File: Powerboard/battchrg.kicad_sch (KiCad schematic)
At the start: 62 parts, among them J1 Thermistor Connection 103AT N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, Q1 SI7617DN-T1-GE3, Q2 SI7617DN-T1-GE3, Q3 SI7617DN-T1-GE3, Q4 SIS412DN-T1-GE3-iclr, Q5 SIS412DN-T1-GE3-iclr

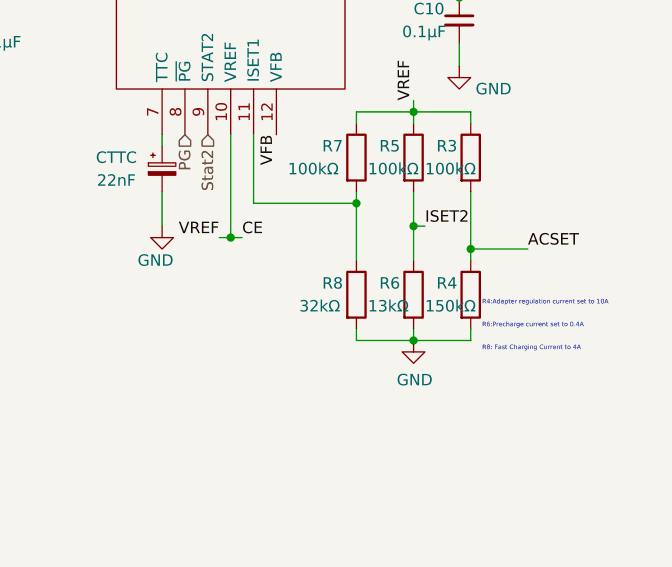
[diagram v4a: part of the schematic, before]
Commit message: removed battery monitor
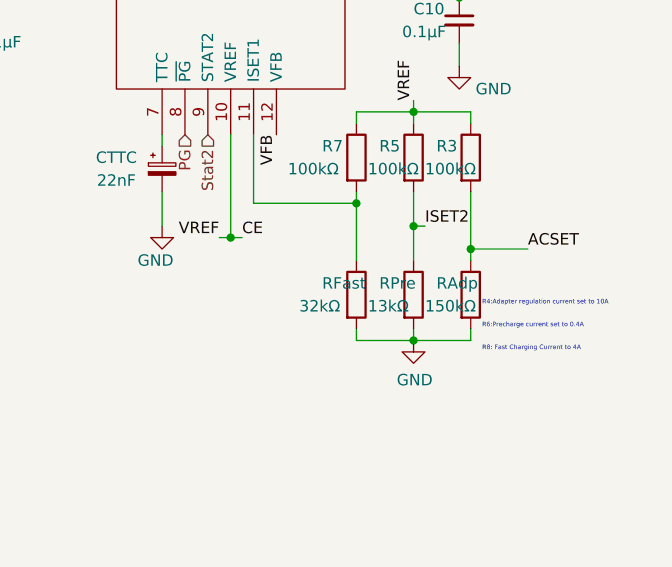
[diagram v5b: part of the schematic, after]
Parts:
- renumbered R4 to RAdp, R8 to RFast, R6 to RPre
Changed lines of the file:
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@@
   (symbol (lib_id "Device:R") (at 241.3 151.13 0) (unit 1)
     (in_bom yes) (on_board yes)
-    (property "Reference" "R8" (id 0) (at 237.49 149.86 0)
+    (property "Reference" "RFast" (id 0) (at 237.49 149.86 0)
       (effects (font (size 1.27 1.27)) (justify left))
     )
@@
   (symbol (lib_id "Device:R") (at 254 151.13 0) (unit 1)
     (in_bom yes) (on_board yes)
-    (property "Reference" "R4" (id 0) (at 250.19 149.86 0)
+    (property "Reference" "RAdp" (id 0) (at 250.19 149.86 0)
       (effects (font (size 1.27 1.27)) (justify left))
     )
@@
   (symbol (lib_id "Device:R") (at 247.65 151.13 0) (unit 1)
     (in_bom yes) (on_board yes)
-    (property "Reference" "R6" (id 0) (at 243.84 149.86 0)
+    (property "Reference" "RPre" (id 0) (at 243.84 149.86 0)
       (effects (font (size 1.27 1.27)) (justify left))
     )

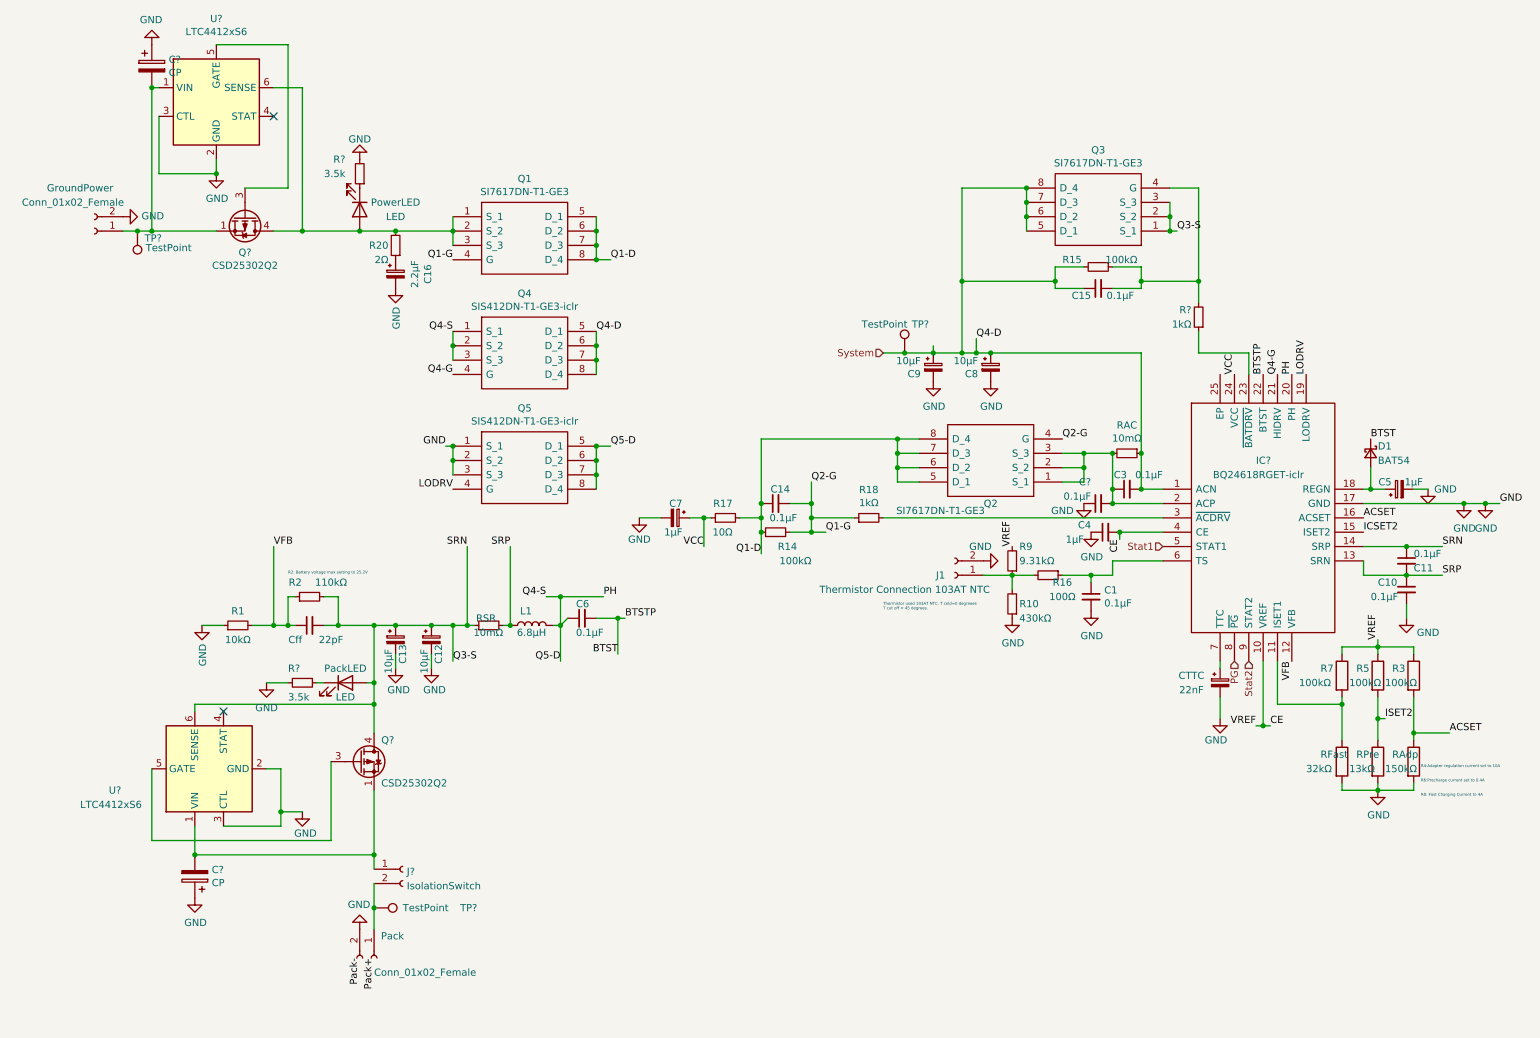
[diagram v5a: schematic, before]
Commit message: Added connectors and potential divider for charge measurement
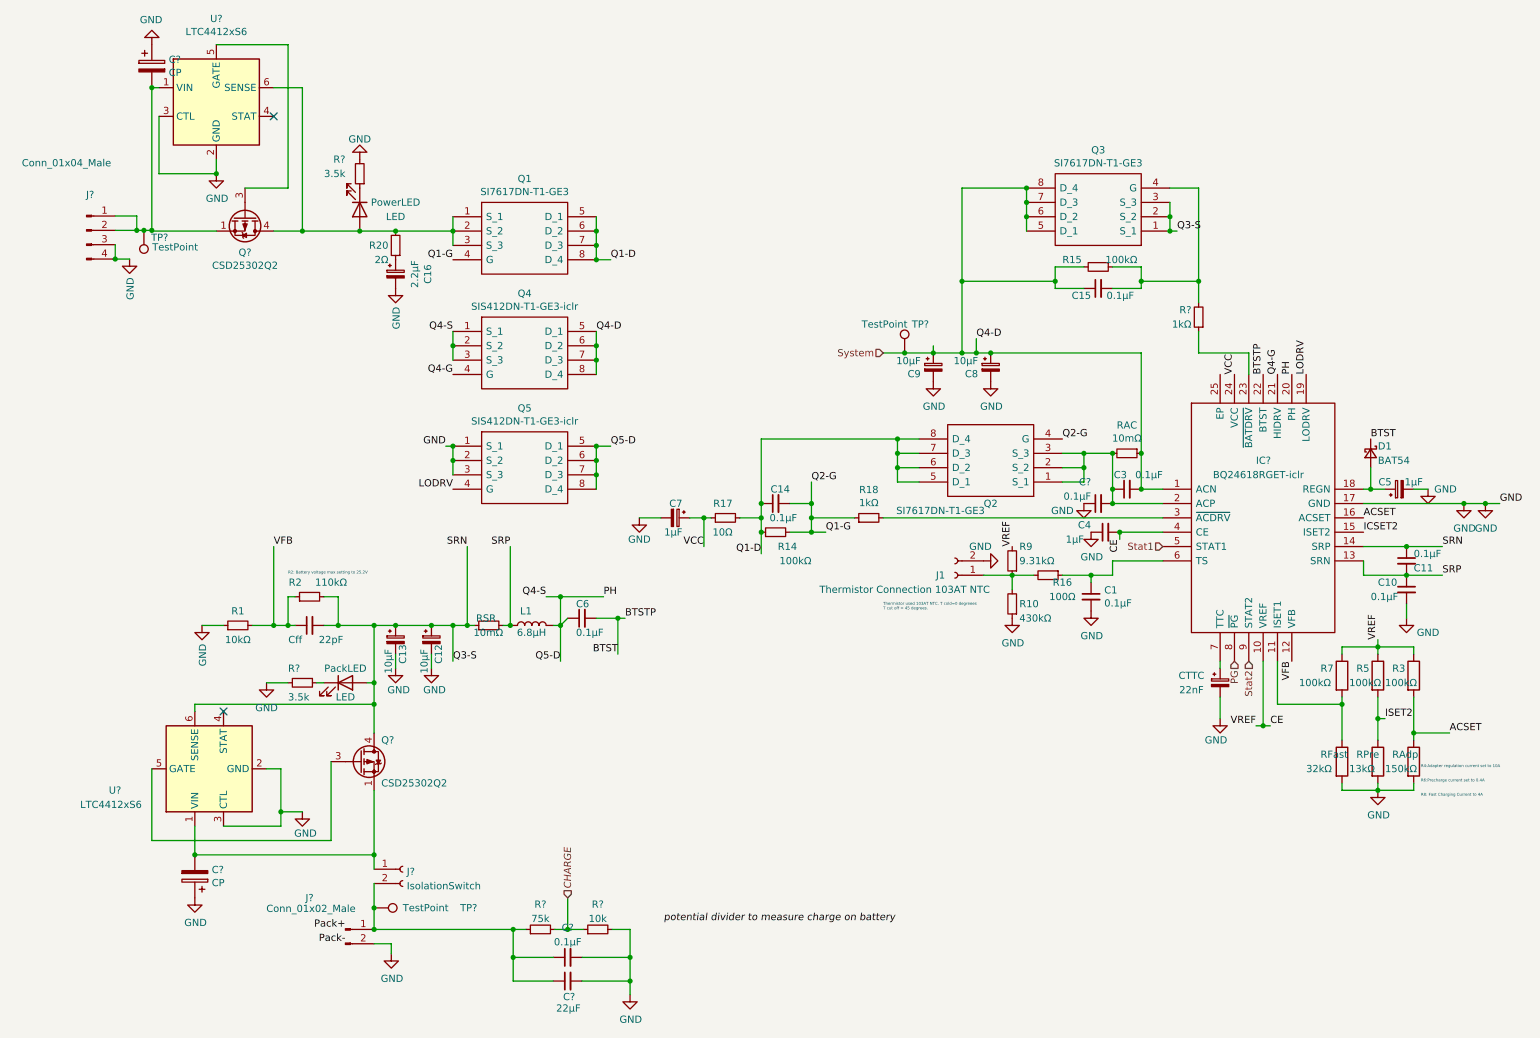
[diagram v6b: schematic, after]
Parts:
- removed GroundPower, Pack: Conn_01x02_Female, symbol Connector:Conn_01x02_Female
- added C?: 0.1μF, symbol Device:C_Small
- added C?: 22μF, symbol Device:C_Small
- added J?: Conn_01x02_Male, Connector_AMASS:AMASS_XT60-M_1x02_P7.20mm_Vertical, symbol Connector:Conn_01x02_Male
- added J?: Conn_01x04_Male, Connector_Molex:Molex_Mini-Fit_Jr_5566-08A2_2x04_P4.20mm_Vertical, symbol Connector:Conn_01x04_Male
- added R?: 75k, symbol Device:R_Small
- added R?: 10k, symbol Device:R_Small
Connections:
- net GND: now also C?.2, C?.2, J?.2 (Pin_2), J?.3 (Pin_3), J?.4 (Pin_4), R?.2
- net at C?.2, Q?.1 (S), Q?.2 (S)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: now also J?.1 (Pin_1), J?.2 (Pin_2)
- net at J?.2 (Pin_2), TP?.1: now also C?.1, C?.1, J?.1 (Pin_1), R?.1
- new net CHARGE: R?.1, R?.2
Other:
- moved on the sheet: TP?

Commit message: removed charger reverse polarity protection
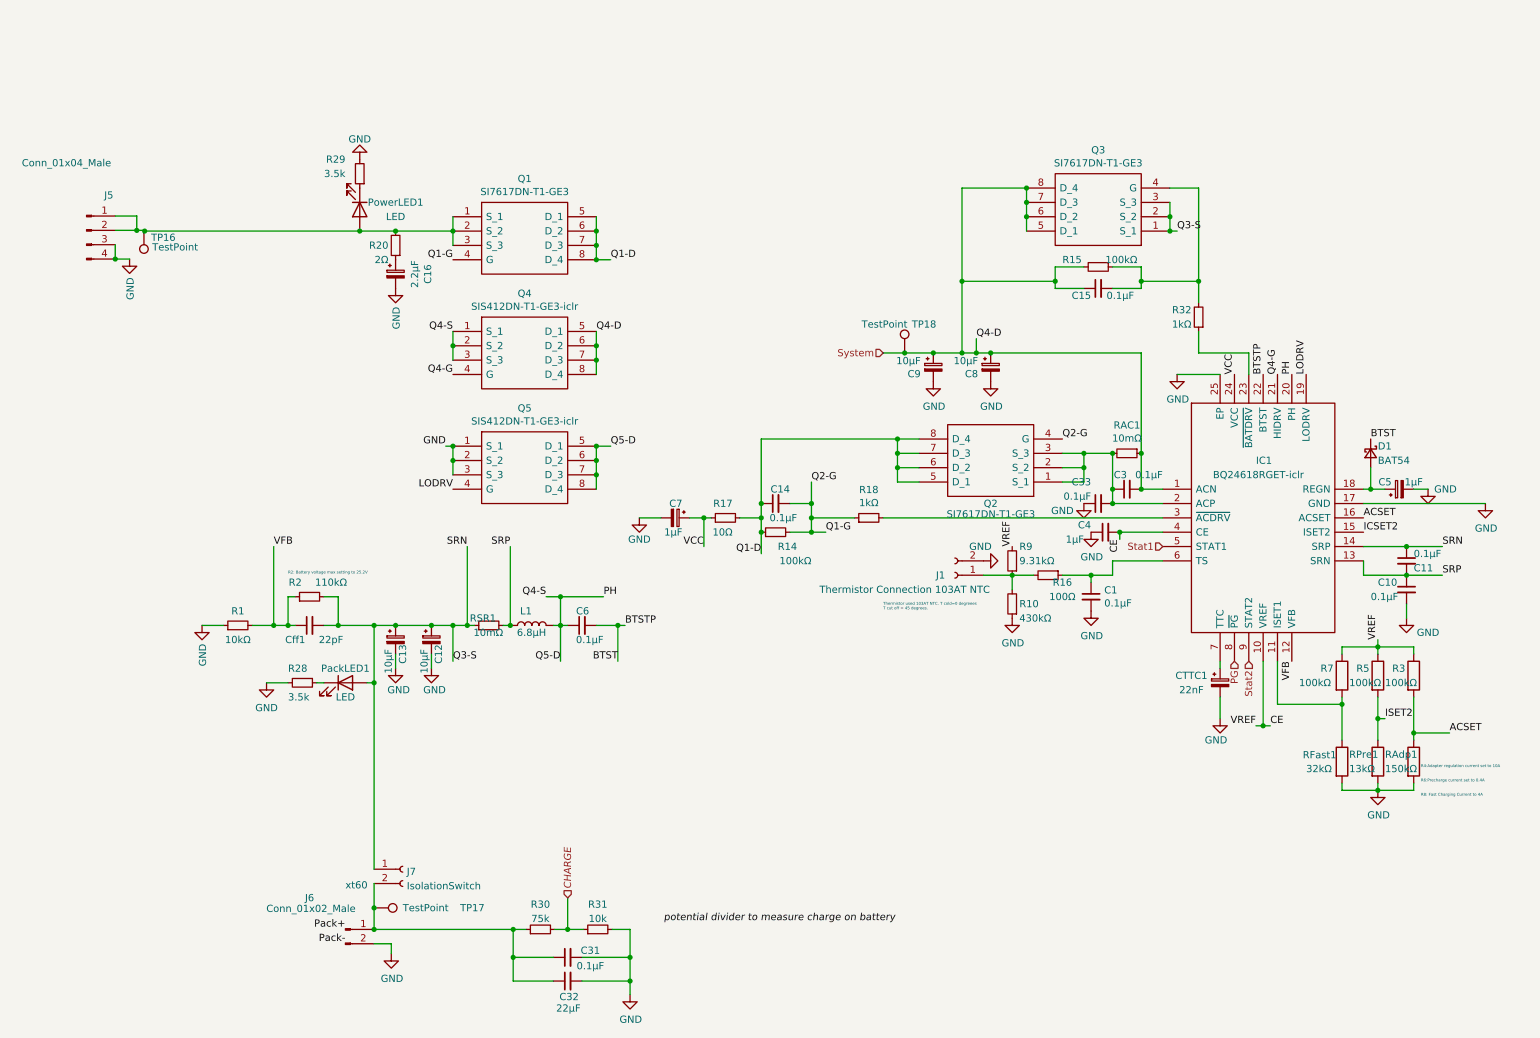
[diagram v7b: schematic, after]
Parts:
- removed C? (x2): CP, symbol Device:CP
- removed Q? (x2): CSD25302Q2, Package_SON:Texas_DQK, symbol Transistor_FET:CSD25302Q2
- removed U? (x2): LTC4412xS6, Package_TO_SOT_SMD:TSOT-23-6, symbol Power_Management:LTC4412xS6
- gave numbers to parts that had none: 15
- renumbered CTTC to CTTC1, Cff to Cff1, PackLED to PackLED1, PowerLED to PowerLED1, RAC to RAC1, RAdp to RAdp1, RFast to RFast1, RPre to RPre1, RSR to RSR1
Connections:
- net GND: now also IC1.25 (EP)
- net Q3-S: now also J7.1 (Pin_1)
- no-connect marks 2 -> 0
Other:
- note added: "xt60"
- moved on the sheet: C6

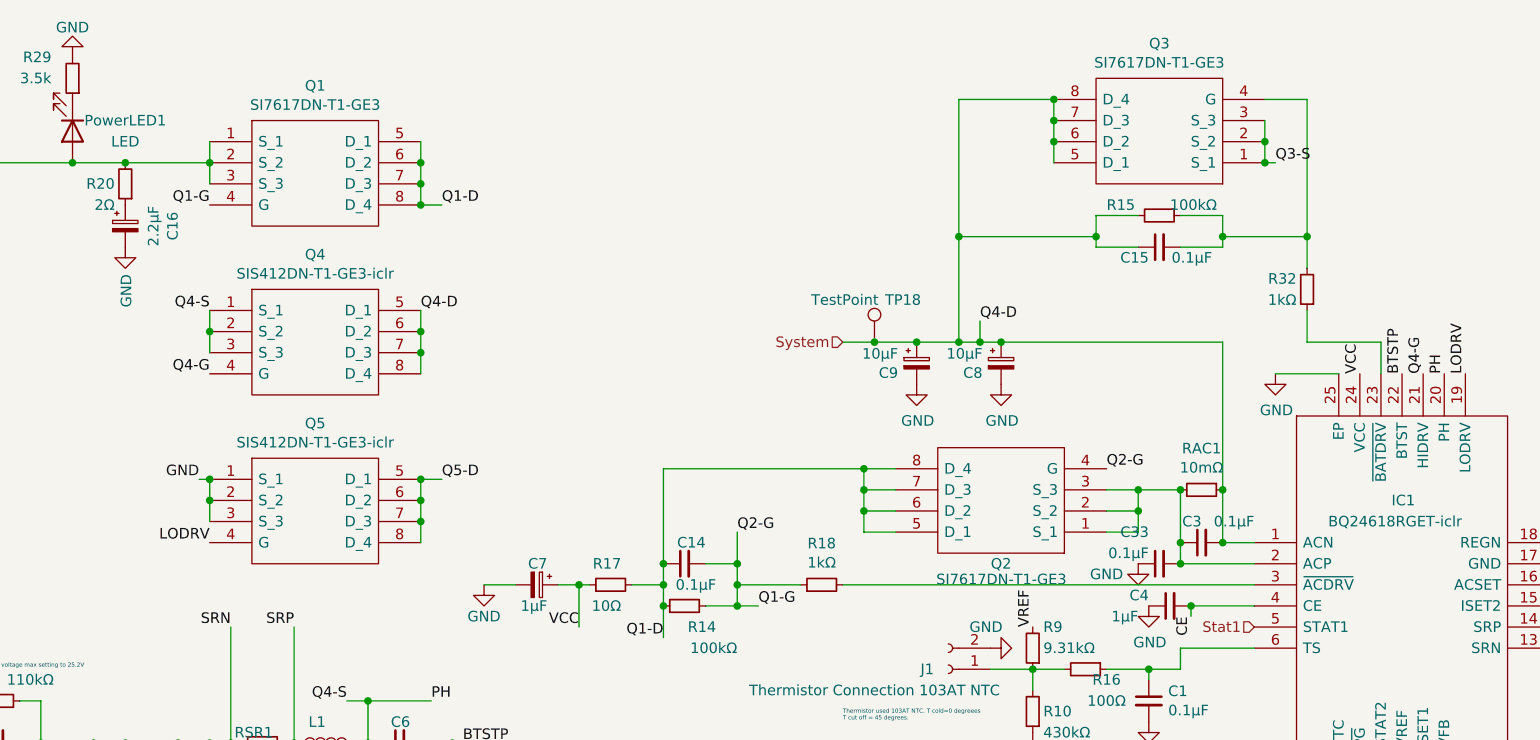
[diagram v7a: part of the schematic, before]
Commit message: changed old mosfets, broke out I2C
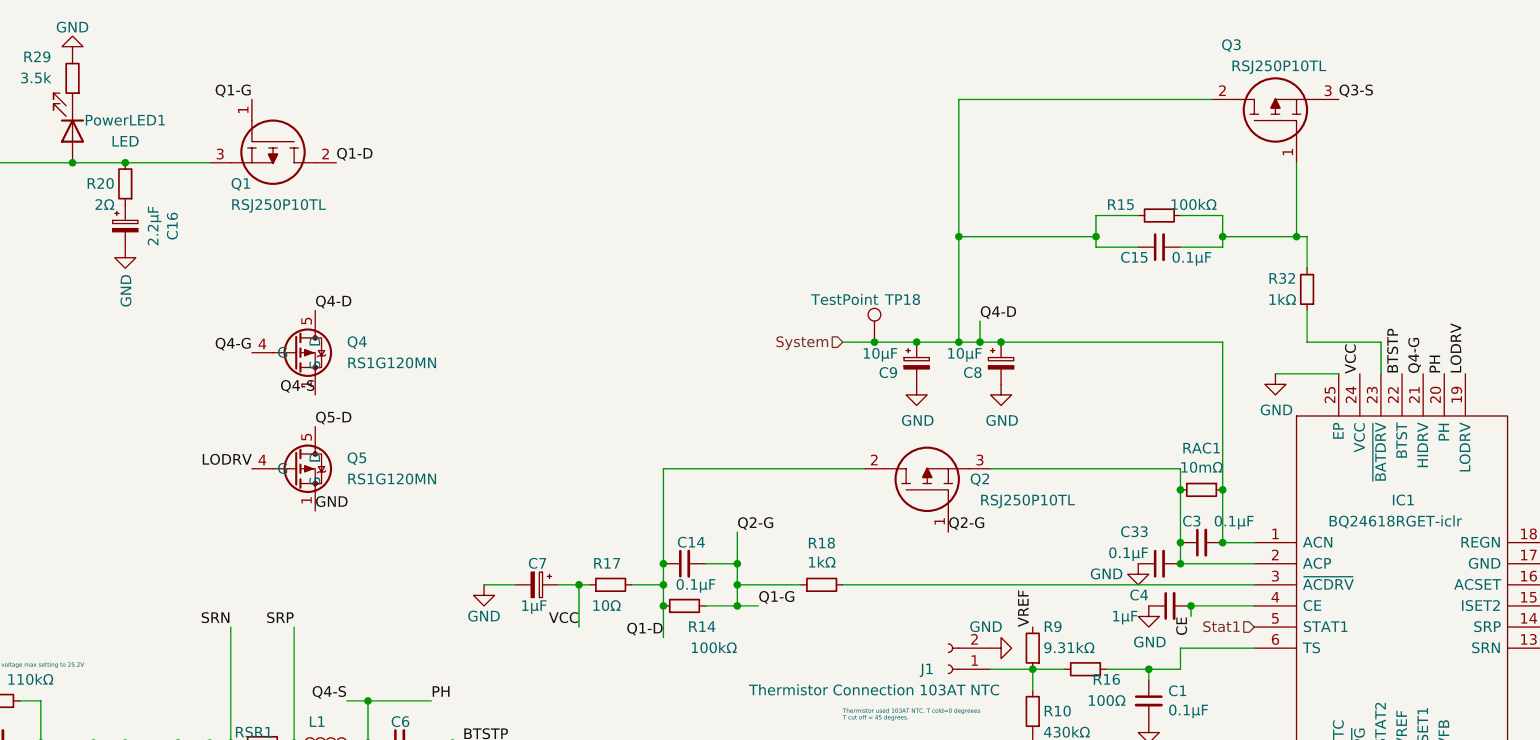
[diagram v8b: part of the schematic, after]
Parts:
- removed Q1, Q2, Q3: SI7617DN-T1-GE3, SIS862DNT1GE3, symbol iclr:SI7617DN-T1-GE3
- removed Q4, Q5: SIS412DN-T1-GE3-iclr, POWERPAK-1212-8, symbol iclr:SIS412DN-T1-GE3-iclr
- added Q1, Q2, Q3: RSJ250P10TL, RSJ151P10TL, symbol iclr:RSJ250P10TL
- added Q4, Q5: RS1G120MN, Package_SO:HSOP-8-1EP_3.9x4.9mm_P1.27mm_EP2.41x3.1mm, symbol iclr:RS1G120MN
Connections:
- net GND: now also Q5.1 (S), Q5.2 (S), Q5.3 (S)
- net LODRV: now also Q5.4 (G)
- net PH: now also Q4.1 (S), Q4.2 (S), Q4.3 (S), Q5.5 (D), Q5.6 (D), Q5.7 (D), Q5.8 (D), Q5.9 (D)
- net Q1-D: now also Q1.2, Q2.2
- net Q1-G: now also Q1.1, Q2.1
- net Q3-S: now also Q3.3
- net Q4-G: now also Q4.4 (G)
- net System: now also Q3.2, Q4.5 (D), Q4.6 (D), Q4.7 (D), Q4.8 (D), Q4.9 (D)
- net at C3.1, C33.2, IC1.2 (ACP)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: now also Q2.3
- net at C15.2, R15.1, R32.2: now also Q3.1
- net at PowerLED1.2 (A), R20.2: now also Q1.3
